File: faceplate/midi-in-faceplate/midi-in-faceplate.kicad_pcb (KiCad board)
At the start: 2 copper layers, 98 x 30 mm, 0 parts

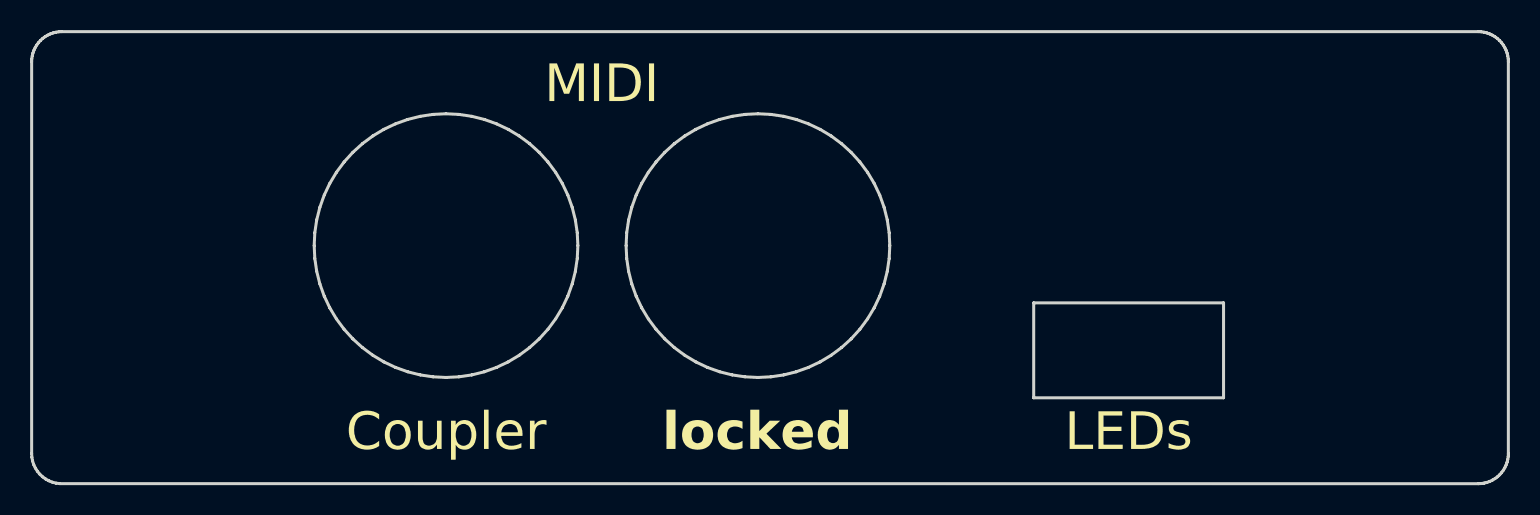
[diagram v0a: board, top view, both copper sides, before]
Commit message: Update faceplates by moving all the holes up 1.6mm
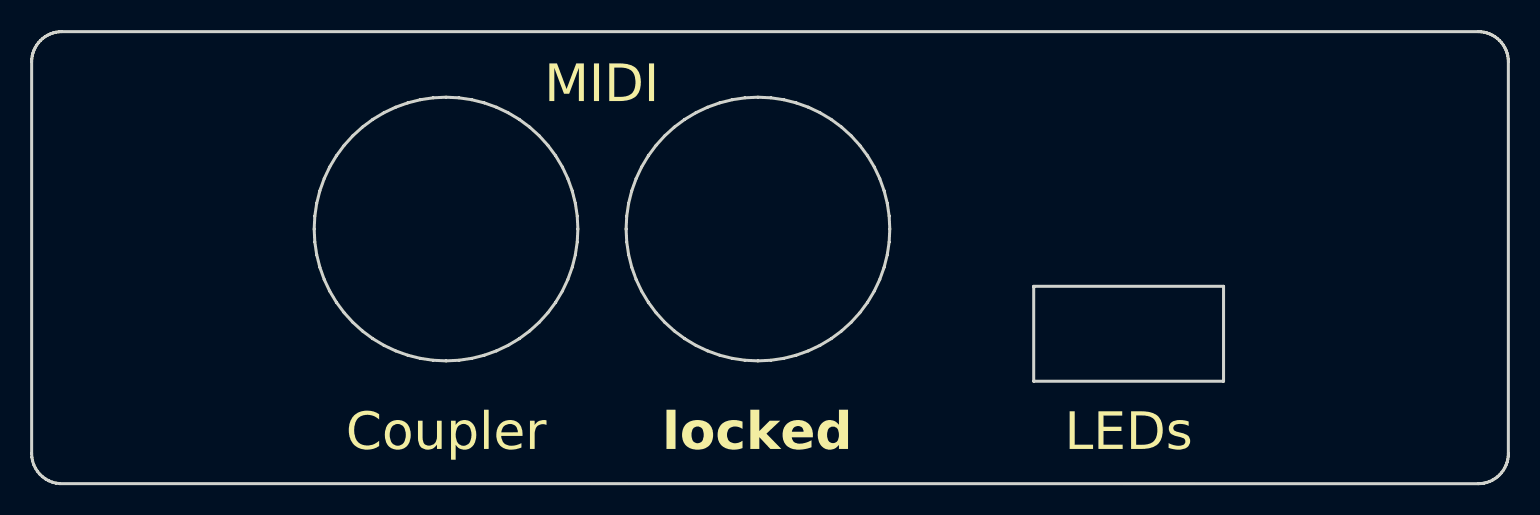
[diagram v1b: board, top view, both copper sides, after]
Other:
- outline, holes or cut-outs redrawn
- board text added: "v2.1.0"
- board text removed: "v2.1.0b1"

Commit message: Update offset around JST connector to 0.2mm (from 0.1mm)
Update version numbers to 3.0.0
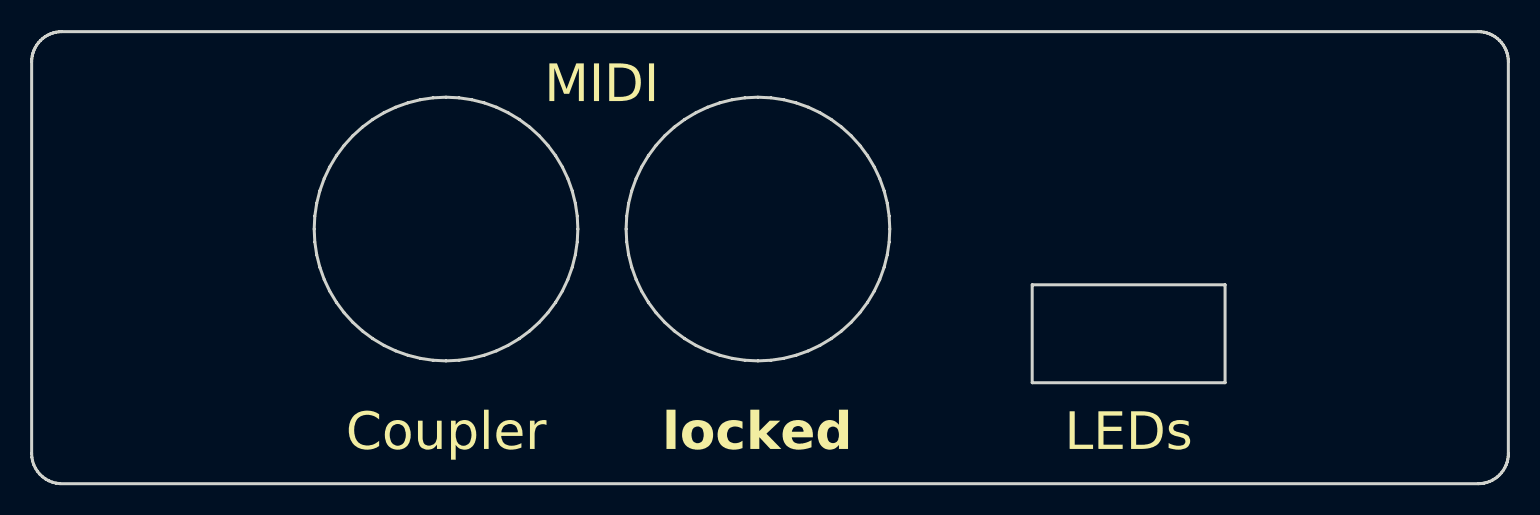
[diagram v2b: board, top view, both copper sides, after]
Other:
- outline, holes or cut-outs redrawn
- board text added: "v3.0.0"
- board text removed: "v2.1.0"
